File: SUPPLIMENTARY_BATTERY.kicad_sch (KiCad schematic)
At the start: 1 part, among them J19 Conn_01x06_Female

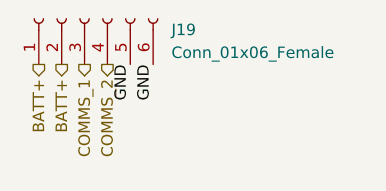
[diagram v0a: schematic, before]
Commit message: mostly routed, need to add more layers fo power and finish low speed signal routing
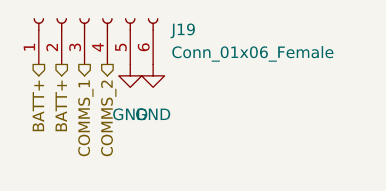
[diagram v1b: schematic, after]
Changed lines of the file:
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@@
 (kicad_sch (version 20210621) (generator eeschema)
   (paper "A4")
-  (label "GND" (at 130.048 71.882 270)
-    (effects (font (size 1.27 1.27)) (justify right bottom))
-  )
-  (label "GND" (at 132.588 71.882 270)
-    (effects (font (size 1.27 1.27)) (justify right bottom))
-  )
   (hierarchical_label "BATT+" (shape output) (at 122.428 71.882 270)
     (effects (font (size 1.27 1.27)) (justify right))
@@
   (hierarchical_label "BATT+" (shape output) (at 119.888 71.882 270)
     (effects (font (size 1.27 1.27)) (justify right))
+  )
+  (symbol (lib_id "power:GND") (at 132.588 71.882 0) (unit 1)
+    (in_bom yes) (on_board yes) (fields_autoplaced)
+    (property "Reference" "#PWR0137" (id 0) (at 132.588 78.232 0)
+      (effects (font (size 1.27 1.27)) hide)
+    )
+    (property "Value" "GND" (id 1) (at 132.588 77.47 0))
+    (property "Footprint" "" (id 2) (at 132.588 71.882 0)
+      (effects (font (size 1.27 1.27)) hide)
+    )
+    (property "Datasheet" "" (id 3) (at 132.588 71.882 0)
+      (effects (font (size 1.27 1.27)) hide)
+    )
+    (pin "1")
   )
   (symbol (lib_id "Connector:Conn_01x06_Female") (at 124.968 66.802 90) (unit 1)
@@
     (pin "6")
   )
+  (symbol (lib_id "power:GND") (at 130.048 71.882 0) (unit 1)
+    (in_bom yes) (on_board yes) (fields_autoplaced)
+    (property "Reference" "#PWR0136" (id 0) (at 130.048 78.232 0)
+      (effects (font (size 1.27 1.27)) hide)
+    )
+    (property "Value" "GND" (id 1) (at 130.048 77.47 0))
+    (property "Footprint" "" (id 2) (at 130.048 71.882 0)
+      (effects (font (size 1.27 1.27)) hide)
+    )
+    (property "Datasheet" "" (id 3) (at 130.048 71.882 0)
+      (effects (font (size 1.27 1.27)) hide)
+    )
+    (pin "1")
+  )
 )
